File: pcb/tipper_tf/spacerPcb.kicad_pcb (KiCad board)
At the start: 2 copper layers, 14 x 48 mm, 5 parts, among them J3 Conn_01x04, J4 Conn_01x04, SW1 SW_Push, SW2 SW_Push, SW3 SW_Push

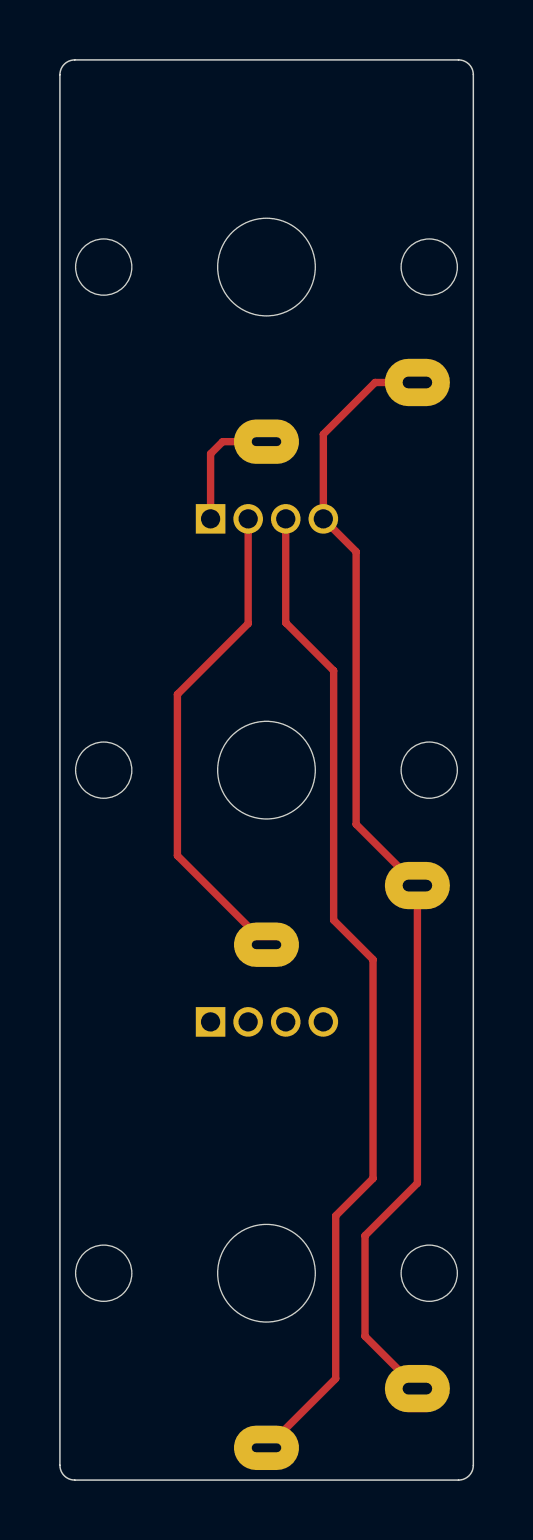
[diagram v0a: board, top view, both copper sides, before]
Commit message: change: spacer and backside pcbs changed to reflect changes in case and main pcb
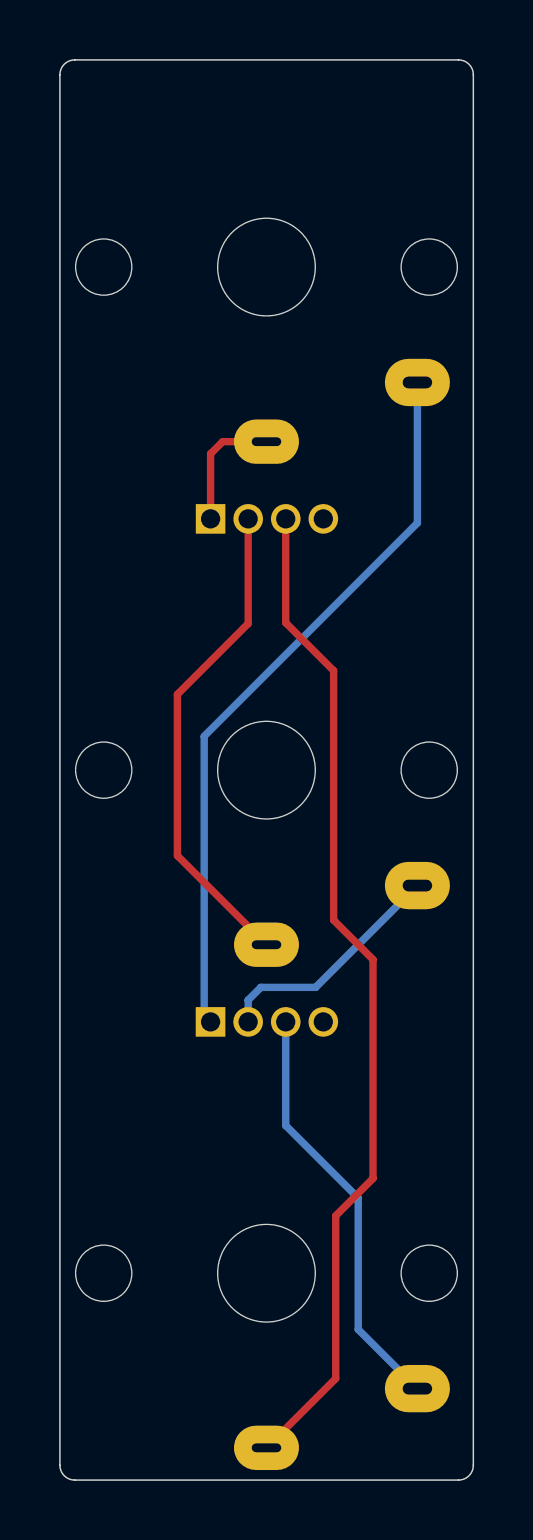
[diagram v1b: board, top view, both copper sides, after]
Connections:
- J3 pad 1: unconnected-(J3-Pad1) -> /Row1
- J3 pad 2: unconnected-(J3-Pad2) -> /Row2
- J3 pad 3: unconnected-(J3-Pad3) -> /Row3
- J4 pad 4: /Col_0 -> (no net)
- SW1 pad 1: /Col_0 -> /Row1
- SW2 pad 1: /Col_0 -> /Row2
- SW3 pad 1: /Col_0 -> /Row3
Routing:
- net /Col_0: track 38.9 -> 0.00 mm
- net /Row1: track 0.00 -> 24.7 mm
- net /Row3: track 0.00 -> 14.2 mm
- net /Row2: track 0.00 -> 8.06 mm
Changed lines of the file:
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@@
-(kicad_pcb (version 20210824) (generator pcbnew)
+(kicad_pcb (version 20210925) (generator pcbnew)
   (general
     (thickness 1.2)
@@
   (net 2 "/LM_sw")
   (net 3 "/LB_sw")
-  (net 4 "/Col_0")
-  (net 5 "unconnected-(J3-Pad1)")
-  (net 6 "unconnected-(J3-Pad2)")
-  (net 7 "unconnected-(J3-Pad3)")
-  (net 8 "unconnected-(J3-Pad4)")
+  (net 4 "/Row1")
+  (net 5 "/Row2")
+  (net 6 "/Row3")
+  (net 7 "unconnected-(J3-Pad4)")
   (footprint "Weteor:Kailh_Choc_1u" locked (layer "B.Cu")
     (at 152.4 73.48 180)
@@
     (pad "" np_thru_hole circle locked (at -5.5 0 90) (size 1.9 1.9) (drill 1.9) (layers *.Cu *.Mask))
     (pad "1" thru_hole oval locked (at -5.1 -3.9 180) (size 2.2 1.6) (drill oval 1 0.4) (layers *.Cu "F.Mask")
-      (net 4 "/Col_0") (pinfunction "1"))
+      (net 4 "/Row1") (pinfunction "1"))
     (pad "2" thru_hole oval locked (at 0 -5.9 180) (size 2.2 1.5) (drill oval 1 0.3) (layers *.Cu "F.Mask")
       (net 1 "/LT_sw") (pinfunction "2"))
@@
     (pad "" np_thru_hole circle locked (at 5.5 0 90) (size 1.9 1.9) (drill 1.9) (layers *.Cu *.Mask))
     (pad "1" thru_hole oval locked (at -5.1 -3.9 180) (size 2.2 1.6) (drill oval 1 0.4) (layers *.Cu "F.Mask")
-      (net 4 "/Col_0") (pinfunction "1") (pintype "passive"))
+      (net 5 "/Row2") (pinfunction "1") (pintype "passive"))
     (pad "2" thru_hole oval locked (at 0 -5.9 180) (size 2.2 1.5) (drill oval 1 0.3) (layers *.Cu "F.Mask")
       (net 2 "/LM_sw") (pinfunction "2") (pintype "passive"))
@@
     (pad "" np_thru_hole circle locked (at 5.5 0 90) (size 1.9 1.9) (drill 1.9) (layers *.Cu *.Mask))
     (pad "1" thru_hole oval locked (at -5.1 -3.9 180) (size 2.2 1.6) (drill oval 1 0.4) (layers *.Cu "F.Mask")
-      (net 4 "/Col_0") (pinfunction "1"))
+      (net 6 "/Row3") (pinfunction "1"))
     (pad "2" thru_hole oval locked (at 0 -5.9 180) (size 2.2 1.5) (drill oval 1 0.3) (layers *.Cu "F.Mask")
       (net 3 "/LB_sw") (pinfunction "2"))
@@
       (net 3 "/LB_sw") (pinfunction "Pin_3"))
     (pad "4" thru_hole oval (at 0 -3.81 270) (size 1 1) (drill 0.65) (layers *.Cu *.Mask)
-      (net 4 "/Col_0") (pinfunction "Pin_4"))
+      (pinfunction "Pin_4"))
     (model "${KISYS3DMOD}/Connector_PinHeader_1.27mm.3dshapes/PinHeader_1x04_P1.27mm_Vertical.wrl"
       (offset (xyz 0 0 0))
@@
     (fp_line (start -1.05 -4.445) (end -1.05 0.11) (layer "B.Fab") (width 0.1))
     (pad "1" thru_hole rect (at 0 0 270) (size 1 1) (drill 0.65) (layers *.Cu *.Mask)
-      (net 5 "unconnected-(J3-Pad1)") (pinfunction "Pin_1"))
+      (net 4 "/Row1") (pinfunction "Pin_1"))
     (pad "2" thru_hole oval (at 0 -1.27 270) (size 1 1) (drill 0.65) (layers *.Cu *.Mask)
-      (net 6 "unconnected-(J3-Pad2)") (pinfunction "Pin_2"))
+      (net 5 "/Row2") (pinfunction "Pin_2"))
     (pad "3" thru_hole oval (at 0 -2.54 270) (size 1 1) (drill 0.65) (layers *.Cu *.Mask)
-      (net 7 "unconnected-(J3-Pad3)") (pinfunction "Pin_3"))
+      (net 6 "/Row3") (pinfunction "Pin_3"))
     (pad "4" thru_hole oval (at 0 -3.81 270) (size 1 1) (drill 0.65) (layers *.Cu *.Mask)
-      (net 8 "unconnected-(J3-Pad4)") (pinfunction "Pin_4"))
+      (net 7 "unconnected-(J3-Pad4)") (pinfunction "Pin_4"))
     (model "${KISYS3DMOD}/Connector_PinHeader_1.27mm.3dshapes/PinHeader_1x04_P1.27mm_Vertical.wrl"
       (offset (xyz 0 0 0))
@@
   (segment (start 153.051391 81.988624) (end 153.051391 85.501391) (width 0.25) (layer "F.Cu") (net 3))
   (segment (start 156 96.88) (end 156 104.28) (width 0.25) (layer "F.Cu") (net 3))
-  (segment (start 157.5 77.38) (end 156.07 77.38) (width 0.25) (layer "F.Cu") (net 4))
-  (segment (start 155.73 106.21) (end 155.73 109.61) (width 0.25) (layer "F.Cu") (net 4))
-  (segment (start 156.07 77.38) (end 154.321391 79.128609) (width 0.25) (layer "F.Cu") (net 4))
-  (segment (start 155.73 109.61) (end 157.5 111.38) (width 0.25) (layer "F.Cu") (net 4))
-  (segment (start 157.5 94.379999) (end 157.5 104.44) (width 0.25) (layer "F.Cu") (net 4))
-  (segment (start 157.5 104.44) (end 155.73 106.21) (width 0.25) (layer "F.Cu") (net 4))
-  (segment (start 154.321391 79.128609) (end 154.321391 81.988624) (width 0.25) (layer "F.Cu") (net 4))
-  (segment (start 155.43 83.097233) (end 155.43 92.309999) (width 0.25) (layer "F.Cu") (net 4))
-  (segment (start 155.43 92.309999) (end 157.5 94.379999) (width 0.25) (layer "F.Cu") (net 4))
-  (segment (start 154.321391 81.988624) (end 155.43 83.097233) (width 0.25) (layer "F.Cu") (net 4))
+  (segment (start 157.5 82.13) (end 157.5 77.38) (width 0.25) (layer "B.Cu") (net 4))
+  (segment (start 150.295479 98.77183) (end 150.295479 89.334521) (width 0.25) (layer "B.Cu") (net 4))
+  (segment (start 150.295479 89.334521) (end 157.5 82.13) (width 0.25) (layer "B.Cu") (net 4))
+  (segment (start 150.510605 98.986956) (end 150.295479 98.77183) (width 0.25) (layer "B.Cu") (net 4))
+  (segment (start 152.21 97.82) (end 154.059999 97.82) (width 0.25) (layer "B.Cu") (net 5))
+  (segment (start 154.059999 97.82) (end 157.5 94.379999) (width 0.25) (layer "B.Cu") (net 5))
+  (segment (start 151.780605 98.249395) (end 152.21 97.82) (width 0.25) (layer "B.Cu") (net 5))
+  (segment (start 151.780605 98.986956) (end 151.780605 98.249395) (width 0.25) (layer "B.Cu") (net 5))
+  (segment (start 155.5 104.94) (end 155.5 109.38) (width 0.25) (layer "B.Cu") (net 6))
+  (segment (start 153.050605 102.490605) (end 155.5 104.94) (width 0.25) (layer "B.Cu") (net 6))
+  (segment (start 153.050605 98.986956) (end 153.050605 102.490605) (width 0.25) (layer "B.Cu") (net 6))
+  (segment (start 155.5 109.38) (end 157.5 111.38) (width 0.25) (layer "B.Cu") (net 6))
 )
